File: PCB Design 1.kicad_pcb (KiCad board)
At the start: 2 copper layers, 27 parts, among them Q1 MMBT3906, Q2 MMBT3906, Q3 MMBT3906, Q4 MMBT3906, Q5 MMBT3906, Q6 MMBT3906, Q7 MMBT3906, Q8 MMBT3906, SW1 SW_PUSH, U1 MAX6969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

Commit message: Second Commit - TL084's left to implement
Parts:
- removed R5, R6, R7, R8, R9: 10K, Resistors_SMD:R_0402
- removed REF** (x4): PINHEAD1-6, Connect:PINHEAD1-6
- added MCU2: MSP430G2353, Housings_DIP:DIP-20_W7.62mm, F.Cu at (105.4, 31.8)
- added R12, R13, R14, R15, R16, R17: 10K, Resistors_SMD:R_0402, F.Cu at (0.00, 0.00)
- added SW2: SW_PUSH, Buttons_Switches_SMD:SW_SPST_EVPBF, F.Cu at (67.3, 53.3)
- added U3: 74HC595, Housings_DIP:DIP-16_W7.62mm, F.Cu at (74.9, 104.1)
- added U4: CD4051B, Housings_DIP:DIP-16_W7.62mm, F.Cu at (52.1, 73.7)
- R2: value 500 -> 47K
- R4: value 10K -> 500
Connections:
- MCU1 pad 11: /~OE~/P2.3 -> /RCLK
- MCU1 pad 12: /CLK/P2.4 -> /SRCLK
- MCU1 pad 13: /LE/P2.5 -> /SER
- MCU1 pad 14: (no net) -> /AnalogInput-(X)
- MCU1 pad 15: (no net) -> /(A)
- MCU1 pad 18: /DIN2/P2.7 -> /(C)
- MCU1 pad 19: /DIN1/P2.6 -> /(B)
- MCU1 pad 3: (no net) -> /SOMI(1)-SIMO(2)
- MCU1 pad 4: (no net) -> /SIMO(1)-SOMI(2)
- MCU1 pad 6: (no net) -> /CLK
- MCU1 pad 7: (no net) -> /CS
- R1 pad 1: Net-(MCU1-Pad16) -> Net-(MCU2-Pad16)
- R10 pad 1: Net-(Q7-Pad1) -> Net-(Q1-Pad1)
- R11 pad 1: Net-(Q8-Pad1) -> Net-(Q2-Pad1)
- R2 pad 1: Net-(R2-Pad1) -> Net-(MCU1-Pad16)
- R2 pad 2: GND -> +3V3
- R4 pad 1: Net-(Q1-Pad1) -> Net-(R4-Pad1)
- R4 pad 2: Net-(R4-Pad2) -> GND
- SW1 pad 1: Net-(MCU1-Pad16) -> Net-(MCU2-Pad16)
- U1 pad 23: Net-(R2-Pad1) -> Net-(R3-Pad1)
- U2 pad 13: Net-(R4-Pad2) -> Net-(R10-Pad2)
- U2 pad 14: Net-(R5-Pad2) -> Net-(R11-Pad2)
- U2 pad 19: Net-(R10-Pad2) -> Net-(R16-Pad2)
- U2 pad 20: Net-(R11-Pad2) -> Net-(R17-Pad2)
- U2 pad 23: Net-(R3-Pad1) -> Net-(R4-Pad1)

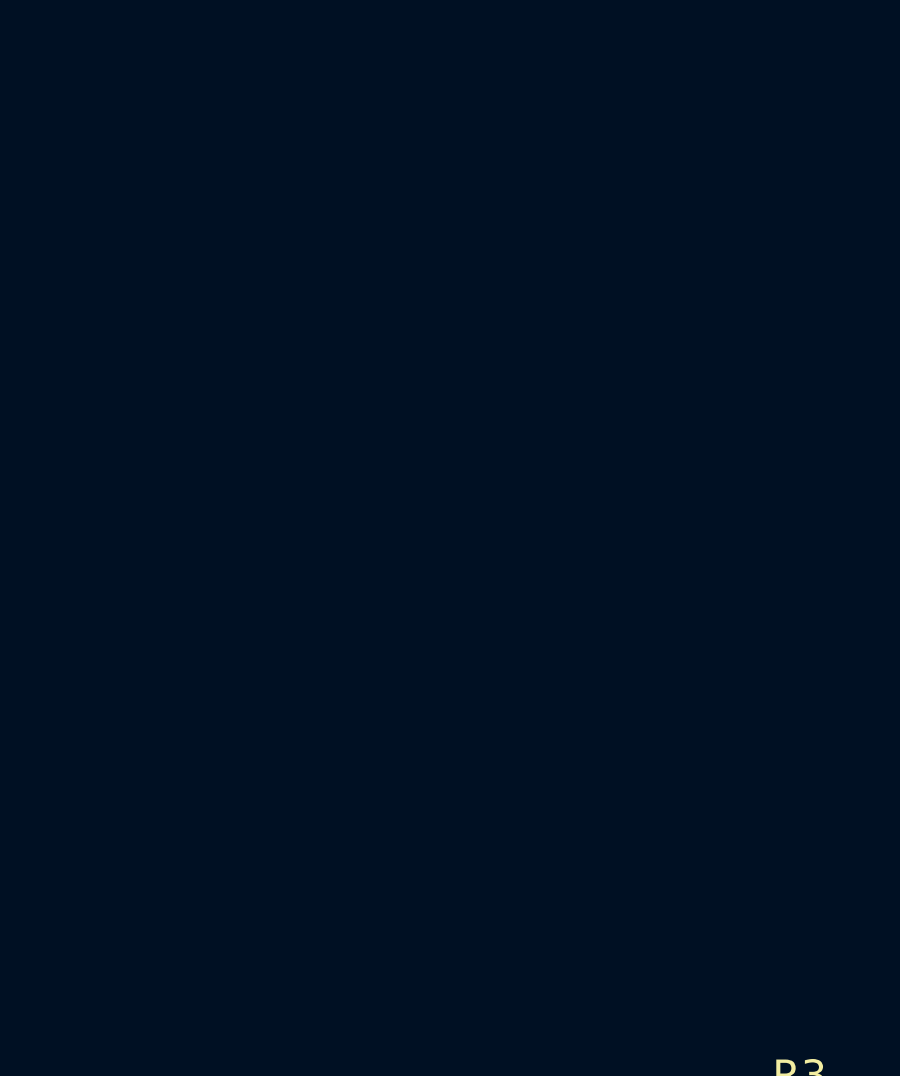
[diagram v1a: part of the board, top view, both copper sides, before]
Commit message: UART Tri-State Buffer Update
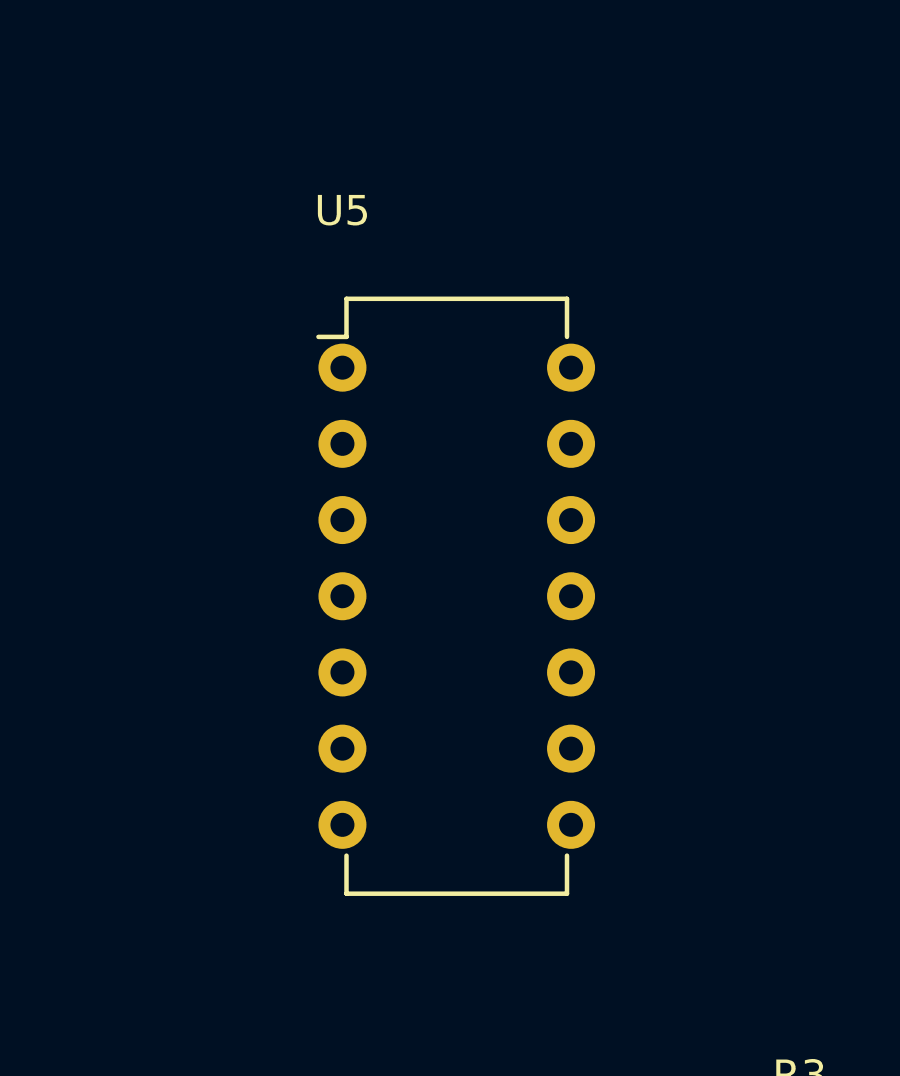
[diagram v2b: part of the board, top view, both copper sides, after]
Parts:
- added U5: 74125/126, Housings_DIP:DIP-14_W7.62mm, F.Cu at (139.7, 43.2)
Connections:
- MCU1 pad 2: (no net) -> /UART(CS)
- MCU2 pad 1: +3V3 -> Net-(MCU2-Pad1)
- R1 pad 2: +3V3 -> Net-(MCU2-Pad1)
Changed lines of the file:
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@@
 (kicad_pcb (version 4) (host pcbnew 4.0.1-stable)
   (general
-    (links 69)
-    (no_connects 66)
+    (links 74)
+    (no_connects 71)
     (area 0 0 0 0)
     (thickness 1.6)
@@
     (tracks 0)
     (zones 0)
-    (modules 28)
-    (nets 40)
+    (modules 29)
+    (nets 42)
   )
   (page A4)
@@
   (net 38 "/(C)")
   (net 39 "/(B)")
+  (net 40 "/UART(CS)")
+  (net 41 "Net-(MCU2-Pad1)")
   (net_class Default "This is the default net class."
     (clearance 0.2)
@@
     (add_net "/SOMI(1)-SIMO(2)")
     (add_net /SRCLK)
+    (add_net "/UART(CS)")
     (add_net /~OE~/P2.3)
     (add_net GND)
     (add_net "Net-(MCU1-Pad16)")
+    (add_net "Net-(MCU2-Pad1)")
     (add_net "Net-(MCU2-Pad16)")
     (add_net "Net-(Q1-Pad1)")
@@
     (pad 1 thru_hole oval (at 0 0) (size 1.6 1.6) (drill 0.8) (layers *.Cu *.Mask F.SilkS)
       (net 1 +3V3))
-    (pad 2 thru_hole oval (at 0 2.54) (size 1.6 1.6) (drill 0.8) (layers *.Cu *.Mask F.SilkS))
+    (pad 2 thru_hole oval (at 0 2.54) (size 1.6 1.6) (drill 0.8) (layers *.Cu *.Mask F.SilkS)
+      (net 40 "/UART(CS)"))
     (pad 3 thru_hole oval (at 0 5.08) (size 1.6 1.6) (drill 0.8) (layers *.Cu *.Mask F.SilkS)
       (net 21 "/SOMI(1)-SIMO(2)"))
@@
       (net 25 "Net-(MCU2-Pad16)"))
     (pad 2 smd rect (at 0.45 0) (size 0.4 0.6) (layers F.Cu F.Paste F.Mask)
-      (net 1 +3V3))
+      (net 41 "Net-(MCU2-Pad1)"))
     (model Resistors_SMD.3dshapes/R_0402.wrl
       (at (xyz 0 0 0))
@@
     (fp_line (start 0.135 -1.025) (end -0.8 -1.025) (layer F.SilkS) (width 0.15))
     (pad 1 thru_hole oval (at 0 0) (size 1.6 1.6) (drill 0.8) (layers *.Cu *.Mask F.SilkS)
-      (net 1 +3V3))
+      (net 41 "Net-(MCU2-Pad1)"))
     (pad 2 thru_hole oval (at 0 2.54) (size 1.6 1.6) (drill 0.8) (layers *.Cu *.Mask F.SilkS))
     (pad 3 thru_hole oval (at 0 5.08) (size 1.6 1.6) (drill 0.8) (layers *.Cu *.Mask F.SilkS)
@@
       (at (xyz 0 0 0))
       (scale (xyz 1 1 1))
+      (rotate (xyz 0 0 0))
+    )
+  )
+  (module Housings_DIP:DIP-14_W7.62mm (layer F.Cu)
+    (at 139.7 43.18)
+    (descr "14-lead dip package, row spacing 7.62 mm (300 mils)")
+    (tags "dil dip 2.54 300")
+    (fp_text reference U5 (at 0 -5.22) (layer F.SilkS)
+      (effects (font (size 1 1) (thickness 0.15)))
+    )
+    (fp_text value 74125/126 (at 0 -3.72) (layer F.Fab)
+      (effects (font (size 1 1) (thickness 0.15)))
+    )
+    (fp_line (start -1.05 -2.45) (end -1.05 17.7) (layer F.CrtYd) (width 0.05))
+    (fp_line (start 8.65 -2.45) (end 8.65 17.7) (layer F.CrtYd) (width 0.05))
+    (fp_line (start -1.05 -2.45) (end 8.65 -2.45) (layer F.CrtYd) (width 0.05))
+    (fp_line (start -1.05 17.7) (end 8.65 17.7) (layer F.CrtYd) (width 0.05))
+    (fp_line (start 0.135 -2.295) (end 0.135 -1.025) (layer F.SilkS) (width 0.15))
+    (fp_line (start 7.485 -2.295) (end 7.485 -1.025) (layer F.SilkS) (width 0.15))
+    (fp_line (start 7.485 17.535) (end 7.485 16.265) (layer F.SilkS) (width 0.15))
+    (fp_line (start 0.135 17.535) (end 0.135 16.265) (layer F.SilkS) (width 0.15))
+    (fp_line (start 0.135 -2.295) (end 7.485 -2.295) (layer F.SilkS) (width 0.15))
+    (fp_line (start 0.135 17.535) (end 7.485 17.535) (layer F.SilkS) (width 0.15))
+    (fp_line (start 0.135 -1.025) (end -0.8 -1.025) (layer F.SilkS) (width 0.15))
+    (pad 1 thru_hole oval (at 0 0) (size 1.6 1.6) (drill 0.8) (layers *.Cu *.Mask F.SilkS))
+    (pad 2 thru_hole oval (at 0 2.54) (size 1.6 1.6) (drill 0.8) (layers *.Cu *.Mask F.SilkS))
+    (pad 3 thru_hole oval (at 0 5.08) (size 1.6 1.6) (drill 0.8) (layers *.Cu *.Mask F.SilkS))
+    (pad 4 thru_hole oval (at 0 7.62) (size 1.6 1.6) (drill 0.8) (layers *.Cu *.Mask F.SilkS))
+    (pad 5 thru_hole oval (at 0 10.16) (size 1.6 1.6) (drill 0.8) (layers *.Cu *.Mask F.SilkS))
+    (pad 6 thru_hole oval (at 0 12.7) (size 1.6 1.6) (drill 0.8) (layers *.Cu *.Mask F.SilkS))
+    (pad 7 thru_hole oval (at 0 15.24) (size 1.6 1.6) (drill 0.8) (layers *.Cu *.Mask F.SilkS)
+      (net 8 GND))
+    (pad 8 thru_hole oval (at 7.62 15.24) (size 1.6 1.6) (drill 0.8) (layers *.Cu *.Mask F.SilkS)
+      (net 21 "/SOMI(1)-SIMO(2)"))
+    (pad 9 thru_hole oval (at 7.62 12.7) (size 1.6 1.6) (drill 0.8) (layers *.Cu *.Mask F.SilkS))
+    (pad 10 thru_hole oval (at 7.62 10.16) (size 1.6 1.6) (drill 0.8) (layers *.Cu *.Mask F.SilkS)
+      (net 40 "/UART(CS)"))
+    (pad 11 thru_hole oval (at 7.62 7.62) (size 1.6 1.6) (drill 0.8) (layers *.Cu *.Mask F.SilkS))
+    (pad 12 thru_hole oval (at 7.62 5.08) (size 1.6 1.6) (drill 0.8) (layers *.Cu *.Mask F.SilkS)
+      (net 22 "/SIMO(1)-SOMI(2)"))
+    (pad 13 thru_hole oval (at 7.62 2.54) (size 1.6 1.6) (drill 0.8) (layers *.Cu *.Mask F.SilkS)
+      (net 40 "/UART(CS)"))
+    (pad 14 thru_hole oval (at 7.62 0) (size 1.6 1.6) (drill 0.8) (layers *.Cu *.Mask F.SilkS)
+      (net 1 +3V3))
+    (model Housings_DIP.3dshapes/DIP-14_W7.62mm.wrl
+      (at (xyz 0 0 0))
+      (scale (xyz 1 1 1))

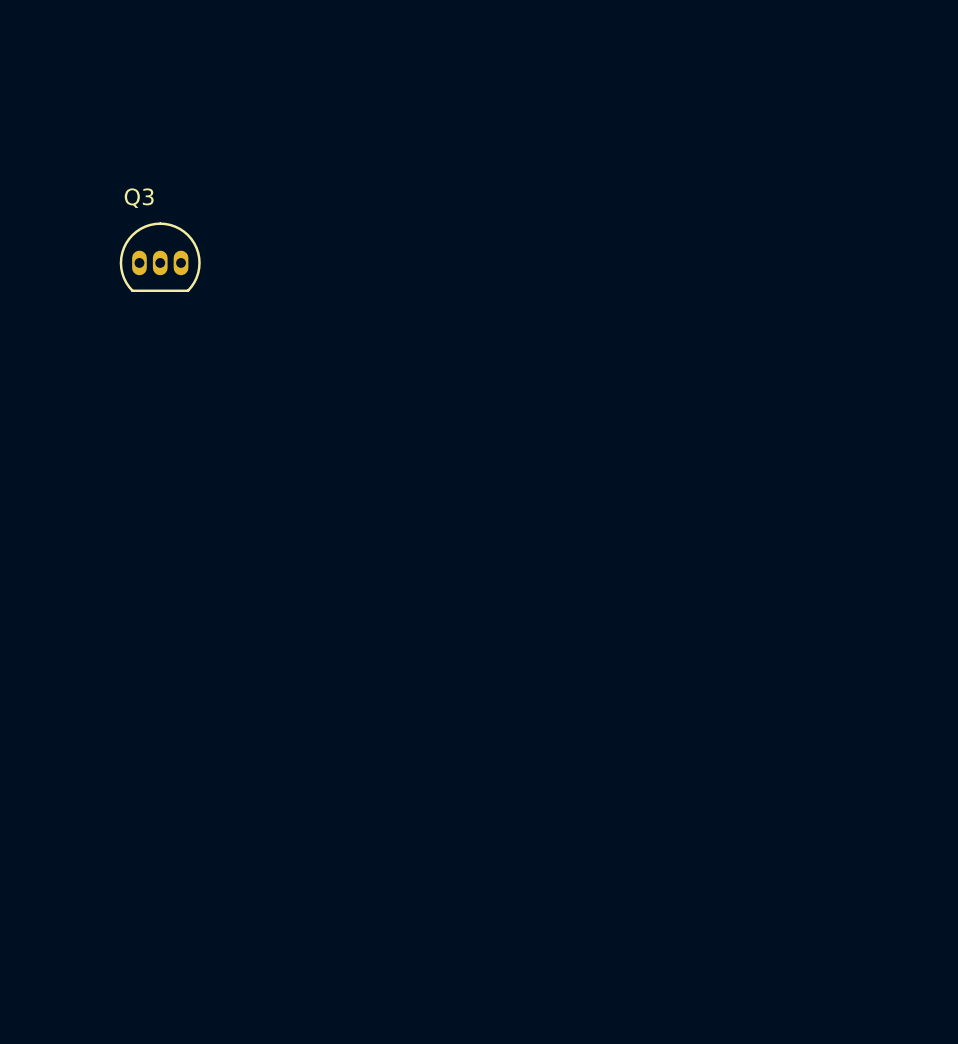
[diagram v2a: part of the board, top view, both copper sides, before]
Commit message: OP AMP Buffer Added
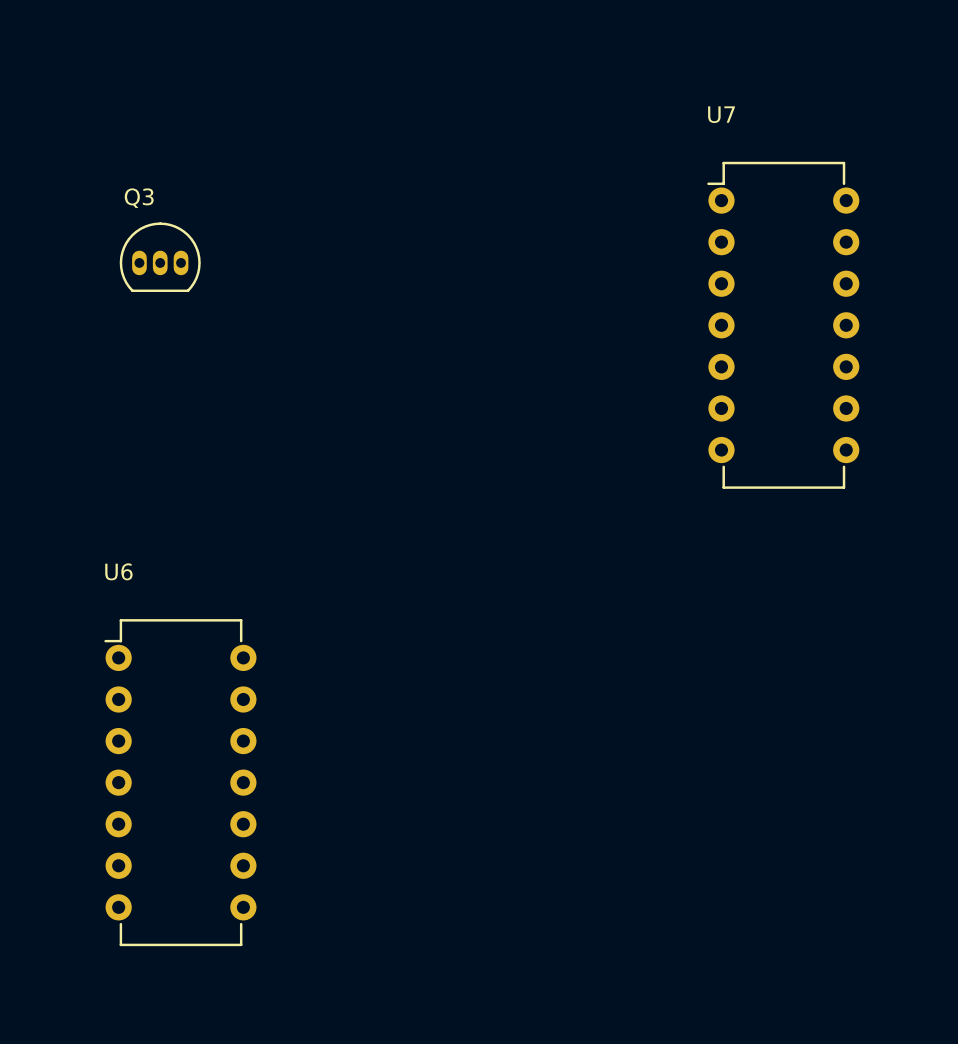
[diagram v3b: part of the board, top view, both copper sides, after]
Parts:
- added U6: TL084, Housings_DIP:DIP-14_W7.62mm, F.Cu at (205.7, 114.3)
- added U7: 74125/126, Housings_DIP:DIP-14_W7.62mm, F.Cu at (242.6, 86.4)
- U5: value 74125/126 -> TL084
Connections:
- MCU1 pad 1: +3V3 -> Net-(MCU1-Pad1)
- R2 pad 2: +3V3 -> Net-(MCU1-Pad1)
- U4 pad 1: (no net) -> Net-(U4-Pad1)
- U4 pad 12: (no net) -> Net-(U4-Pad12)
- U4 pad 13: (no net) -> Net-(U4-Pad13)
- U4 pad 14: (no net) -> Net-(U4-Pad14)
- U4 pad 15: (no net) -> Net-(U4-Pad15)
- U4 pad 2: (no net) -> Net-(U4-Pad2)
- U4 pad 4: (no net) -> Net-(U4-Pad4)
- U4 pad 5: (no net) -> Net-(U4-Pad5)
- U5 pad 1: (no net) -> Net-(U4-Pad13)
- U5 pad 10: /UART(CS) -> (no net)
- U5 pad 11: (no net) -> GND
- U5 pad 12: /SIMO(1)-SOMI(2) -> (no net)
- U5 pad 13: /UART(CS) -> Net-(U4-Pad12)
- U5 pad 14: +3V3 -> Net-(U4-Pad12)
- U5 pad 2: (no net) -> Net-(U4-Pad13)
- U5 pad 4: (no net) -> +5V
- U5 pad 6: (no net) -> Net-(U4-Pad14)
- U5 pad 7: GND -> Net-(U4-Pad14)
- U5 pad 8: /SOMI(1)-SIMO(2) -> Net-(U4-Pad15)
- U5 pad 9: (no net) -> Net-(U4-Pad15)
